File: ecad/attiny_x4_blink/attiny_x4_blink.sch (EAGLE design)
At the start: 3 parts

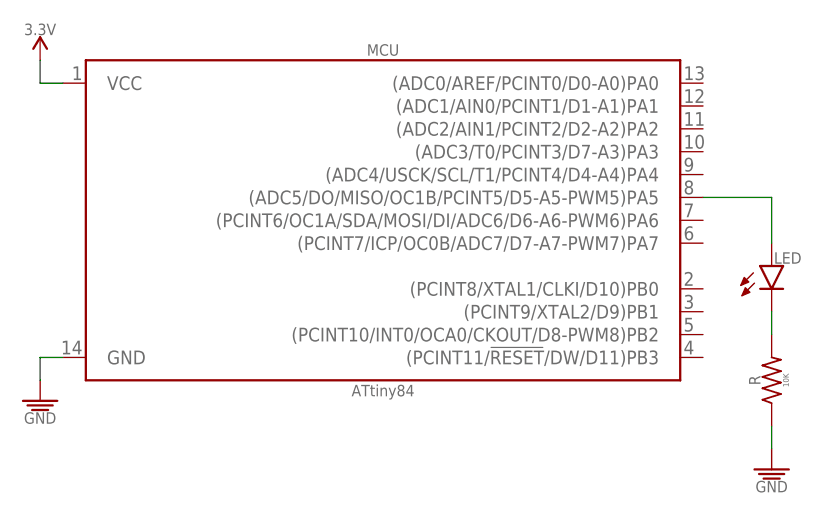
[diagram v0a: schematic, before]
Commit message: Update ATtiny84 symbol to match the CCW ATtiny core.
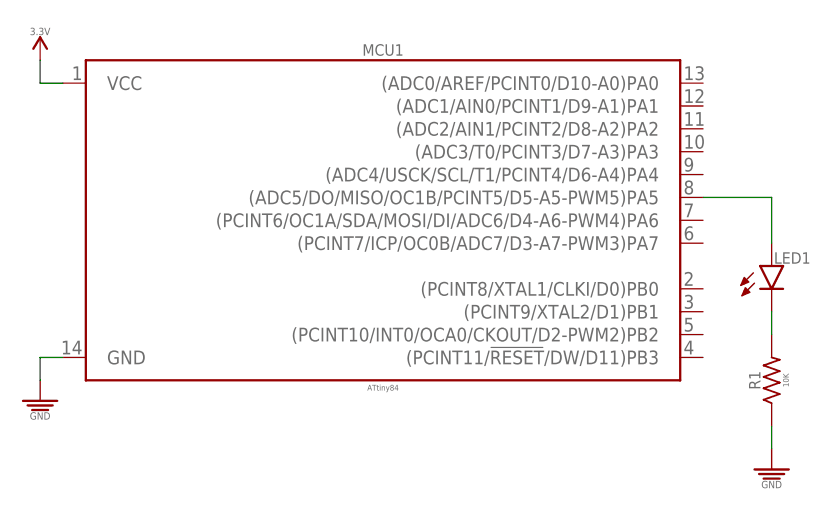
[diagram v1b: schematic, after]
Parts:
- removed LED: (no value), PiB_leds:LED_PTH-5MM_NO-COLOR
- removed R: 10K, PiB_resistors:10KΩ_PTH-207/7_1/4W-5%
- added LED1: (no value), PiB_leds:LED_PTH_T-1_3/4_5MM_NO-COLOR
- added R1: 10K, PiB_resistors:10KΩ_PTH-204/7_1/6W-5%
- renumbered MCU to MCU1
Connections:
- net GND: now also R1.1; no longer R.1
- net N$1: now also LED1.A; no longer LED.A
- net N$2: now also LED1.K, R1.2; no longer LED.K, R.2
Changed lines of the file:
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@@
 <?xml version="1.0" encoding="utf-8"?>
 <!DOCTYPE eagle SYSTEM "eagle.dtd">
-<eagle version="9.1.1">
+<eagle version="9.2.2">
 <drawing>
 <settings>
@@
 <attribute name="SPICEPREFIX" value="G"/>
 </part>
-<part name="LED" library="PiB_leds" deviceset="LED" device="_PTH-5MM_NO-COLOR"/>
-<part name="R" library="PiB_resistors" deviceset="10KΩ" device="_PTH-207/7_1/4W-5%" package3d_urn="urn:adsk.eagle:package:4254576/1" value="10K"/>
+<part name="LED1" library="PiB_leds" deviceset="LED" device="_PTH_T-1_3/4_5MM_NO-COLOR" package3d_urn="urn:adsk.eagle:package:4254847/2"/>
+<part name="R1" library="PiB_resistors" deviceset="10KΩ" device="_PTH-204/7_1/6W-5%" package3d_urn="urn:adsk.eagle:package:4254914/1" value="10K"/>
 <part name="SUPPLY2" library="PiB_power_symbols" deviceset="GND" device=""/>
-<part name="MCU" library="PiB_ic_microcontrollers" deviceset="ATTINY-X4" device="_DIP-14_ATTINY-84" package3d_urn="urn:adsk.eagle:package:3660575/1" value="ATtiny84"/>
+<part name="MCU1" library="PiB_ic_microcontrollers" deviceset="ATTINY-X4" device="_DIP-14_ATTINY-84" package3d_urn="urn:adsk.eagle:package:3660575/1" value="ATtiny84"/>
 </parts>
 <sheets>
@@
 </plain>
 <instances>
-<instance part="SUPPLY1" gate="GND" x="12.7" y="10.16"/>
-<instance part="SUPPLY4" gate="3.3V" x="12.7" y="48.26"/>
-<instance part="LED" gate="G$1" x="93.98" y="25.4"/>
-<instance part="R" gate="G$1" x="93.98" y="12.7" rot="R90"/>
-<instance part="SUPPLY2" gate="GND" x="93.98" y="2.54"/>
-<instance part="MCU" gate="G$1" x="50.8" y="30.48"/>
+<instance part="SUPPLY1" gate="GND" x="12.7" y="10.16" smashed="yes"/>
+<instance part="SUPPLY4" gate="3.3V" x="12.7" y="48.26" smashed="yes"/>
+<instance part="LED1" gate="G$1" x="93.98" y="25.4" smashed="yes">
+<attribute name="NAME" x="94.234" y="25.654" size="1.27" layer="95" font="vector" ratio="10"/>
+<attribute name="VALUE" x="94.234" y="22.606" size="0.635" layer="96" font="vector" ratio="10" align="top-left"/>
+</instance>
+<instance part="R1" gate="G$1" x="93.98" y="12.7" smashed="yes" rot="R90">
+<attribute name="VALUE" x="95.25" y="12.7" size="0.635" layer="96" font="vector" ratio="10" rot="R90" align="top-center"/>
+<attribute name="NAME" x="92.7354" y="12.7" size="1.27" layer="95" font="vector" ratio="10" rot="R90" align="bottom-center"/>
+</instance>
+<instance part="SUPPLY2" gate="GND" x="93.98" y="2.54" smashed="yes"/>
+<instance part="MCU1" gate="G$1" x="50.8" y="30.48" smashed="yes">
+<attribute name="VALUE" x="50.8" y="12.192" size="0.635" layer="96" font="vector" ratio="10" align="top-center"/>
+<attribute name="NAME" x="50.8" y="48.768" size="1.27" layer="95" font="vector" ratio="10" align="bottom-center"/>
+</instance>
 </instances>
 <busses>
@@
 <wire x1="12.7" y1="15.24" x2="15.24" y2="15.24" width="0.1524" layer="91"/>
 <pinref part="SUPPLY1" gate="GND" pin="GND"/>
-<pinref part="MCU" gate="G$1" pin="GND"/>
-</segment>
-<segment>
-<pinref part="R" gate="G$1" pin="1"/>
+<pinref part="MCU1" gate="G$1" pin="GND"/>
+</segment>
+<segment>
+<pinref part="R1" gate="G$1" pin="1"/>
 <pinref part="SUPPLY2" gate="GND" pin="GND"/>
 <wire x1="93.98" y1="5.08" x2="93.98" y2="7.62" width="0.1524" layer="91"/>
@@
 <wire x1="12.7" y1="45.72" x2="12.7" y2="48.26" width="0.1524" layer="91"/>
 <pinref part="SUPPLY4" gate="3.3V" pin="3.3V"/>
-<pinref part="MCU" gate="G$1" pin="VCC"/>
+<pinref part="MCU1" gate="G$1" pin="VCC"/>
 </segment>
 </net>
@@
 <wire x1="86.36" y1="33.02" x2="93.98" y2="33.02" width="0.1524" layer="91"/>
 <wire x1="93.98" y1="33.02" x2="93.98" y2="27.94" width="0.1524" layer="91"/>
-<pinref part="LED" gate="G$1" pin="A"/>
-<pinref part="MCU" gate="G$1" pin="(ADC5/DO/MISO/OC1B/PCINT5/D5-A5-PWM5)PA5"/>
+<pinref part="LED1" gate="G$1" pin="A"/>
+<pinref part="MCU1" gate="G$1" pin="(ADC5/DO/MISO/OC1B/PCINT5/D5-A5-PWM5)PA5"/>
 </segment>
 </net>
 <net name="N$2" class="0">
 <segment>
-<pinref part="LED" gate="G$1" pin="K"/>
+<pinref part="LED1" gate="G$1" pin="K"/>
 <wire x1="93.98" y1="20.32" x2="93.98" y2="17.78" width="0.1524" layer="91"/>
-<pinref part="R" gate="G$1" pin="2"/>
-</segment>
-</net>
+<pinref part="R1" gate="G$1" pin="2"/>
+</segment>
+</net>

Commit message: Update ATtiny84 blink schematic image.
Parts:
- LED1: device PiB_leds:LED_PTH_T-1_3/4_5MM_NO-COLOR -> _leds:LED_PTH_T-1_3/4_5MM_NO-COLOR
- MCU1: device PiB_ic_microcontrollers:ATTINY-X4_DIP-14_ATTINY-84 -> _ic_microcontrollers:ATTINY-X4_DIP-14_ATTINY-84_CONNECTOR
- R1: device PiB_resistors:10KΩ_PTH-204/7_1/6W-5% -> _resistors:10KΩ_PTH-204/7_1/6W-5%
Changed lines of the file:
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@@
 <?xml version="1.0" encoding="utf-8"?>
 <!DOCTYPE eagle SYSTEM "eagle.dtd">
-<eagle version="9.2.2">
+<eagle version="9.3.0">
 <drawing>
 <settings>
@@
 </classes>
 <parts>
-<part name="SUPPLY1" library="PiB_power_symbols" deviceset="GND" device="">
+<part name="SUPPLY1" library="_power_symbols" deviceset="GND" device="">
 <attribute name="SPICEPREFIX" value="G"/>
 </part>
-<part name="SUPPLY4" library="PiB_power_symbols" deviceset="3.3V" device="">
+<part name="SUPPLY4" library="_power_symbols" deviceset="3.3V" device="">
 <attribute name="SPICEPREFIX" value="G"/>
 </part>
-<part name="LED1" library="PiB_leds" deviceset="LED" device="_PTH_T-1_3/4_5MM_NO-COLOR" package3d_urn="urn:adsk.eagle:package:4254847/2"/>
-<part name="R1" library="PiB_resistors" deviceset="10KΩ" device="_PTH-204/7_1/6W-5%" package3d_urn="urn:adsk.eagle:package:4254914/1" value="10K"/>
-<part name="SUPPLY2" library="PiB_power_symbols" deviceset="GND" device=""/>
-<part name="MCU1" library="PiB_ic_microcontrollers" deviceset="ATTINY-X4" device="_DIP-14_ATTINY-84" package3d_urn="urn:adsk.eagle:package:3660575/1" value="ATtiny84"/>
+<part name="LED1" library="_leds" deviceset="LED" device="_PTH_T-1_3/4_5MM_NO-COLOR" package3d_urn="urn:adsk.eagle:package:4254847/2"/>
+<part name="R1" library="_resistors" deviceset="10KΩ" device="_PTH-204/7_1/6W-5%" package3d_urn="urn:adsk.eagle:package:4254914/1" value="10K"/>
+<part name="SUPPLY2" library="_power_symbols" deviceset="GND" device=""/>
+<part name="MCU1" library="_ic_microcontrollers" deviceset="ATTINY-X4" device="_DIP-14_ATTINY-84_CONNECTOR" package3d_urn="urn:adsk.eagle:package:3660578/2" value="ATtiny84"/>
 </parts>
 <sheets>
